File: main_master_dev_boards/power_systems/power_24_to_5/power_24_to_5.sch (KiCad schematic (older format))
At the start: 23 parts, among them J1 Switch_in, J2 24_in, J3 GND_in, J4 PGood_out, J5 ref_out, J6 5_out, J7 GND_out, U1 LMR16030

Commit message: Started Adding 3v3 power LDO to 24_to_5 dev board
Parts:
- added C5: 22uF, Capacitors_SMD:C_0603, symbol C
- added C6: 22uF, Capacitors_SMD:C_0603, symbol CP1
- added D3: GRN_LED, LEDs:LED_0603, symbol LED-RESCUE-main_master_board
- added J8: 3v3_out, Pin_Headers:Pin_Header_Straight_1x01_Pitch2.54mm, symbol CONN_01X01
- added J9: PGoodBackup_out, Pin_Headers:Pin_Header_Straight_1x01_Pitch2.54mm, symbol CONN_01X01
- added R8: 10, Resistors_SMD:R_0603, symbol R
- added U2: 74AUC1G32, SO-70:SO-70, symbol 74AUC1G32
- added U3: LP3852-3.3, SOT-223:SOT-223, symbol LP3852-3.3
- J4: value PGood_out -> PGoodMain_out
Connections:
- net labels added: 3V3, 3V3_out, PG_v5_backup, v5_good
- wire segments 49 -> 67
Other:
- note added: "5V to 3.3V LDO"
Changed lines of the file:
@@
 LIBS:contrib
 LIBS:valves
-LIBS:antenna
-LIBS:AS1360
-LIBS:conn_2x45
-LIBS:conn_2x50
-LIBS:conn_open_q_x2
-LIBS:esd7c5
-LIBS:FDS4935A
-LIBS:FPF1203LUCX
-LIBS:lan9512
-LIBS:LMR16020
-LIBS:LP3852-3.3
-LIBS:LTC2955-1
-LIBS:MIC2026
-LIBS:Si1077X
-LIBS:Si1900DL
-LIBS:SN74LV1T125
-LIBS:SN74LV4T125
-LIBS:TDP6E001RSER
-LIBS:tps82084sil
-LIBS:TPS754
-LIBS:TPS61089
-LIBS:TPS61232DRC
-LIBS:TPS832130SIL
-LIBS:0s102011ma1qn1
-LIBS:74LVC1G17
-LIBS:74V1T126
-LIBS:acs711klctr-12ab-t
-LIBS:AD7192
-LIBS:AD7193
-LIBS:am-hrr30-xxx
-LIBS:aon7528
-LIBS:AP7363
-LIBS:AS1359
-LIBS:csd16323q3
-LIBS:dmn2004dmk
-LIBS:dp_devices
-LIBS:DSPIC33E128MC506
-LIBS:fds6898az
-LIBS:ina197
-LIBS:irf7329pbf
-LIBS:ld1117
-LIBS:lm3478
-LIBS:lm3481
-LIBS:lt1910
-LIBS:ltc1871
-LIBS:ltc1982
-LIBS:MAG3110
-LIBS:mcp1700
-LIBS:mcp73831
-LIBS:mcsmt-g5030a1-3712
-LIBS:microchip_can
-LIBS:microclasp_hdrx2
-LIBS:microclasp_hdrx3
-LIBS:MPU-6000_MPU-6050
-LIBS:MPU-9150
-LIBS:nrf24l01+
-LIBS:pds1040l
-LIBS:pic12f1571
-LIBS:pinhead
-LIBS:psmn013-80ys
-LIBS:RESISTOR_ARRAY
-LIBS:rf803d
-LIBS:RGB_LED
-LIBS:Si1970DH
-LIBS:sn65hvd232
-LIBS:ssc54
-LIBS:sw_push_4
-LIBS:tc74
-LIBS:tps54540
-LIBS:TPS2113A
-LIBS:vs-mbrb1635pbf
-LIBS:xal5050-562meb
-LIBS:xal6030-182mec
-LIBS:ld29150dt50r
-LIBS:ncp59151ds50r4g
-LIBS:pinhd-2x23
+LIBS:main_master_board-cache
 LIBS:power_24_to_5-cache
 EELAYER 25 0
@@
 P 7740 3790
 F 0 "J4" H 7740 3890 50  0000 C CNN
-F 1 "PGood_out" V 7840 3790 50  0000 C CNN
+F 1 "PGoodMain_out" V 7840 3790 50  0000 C CNN
 F 2 "Pin_Headers:Pin_Header_Straight_1x01_Pitch2.54mm" H 7740 3790 50  0001 C CNN
 F 3 "" H 7740 3790 50  0001 C CNN
@@
 Wire Wire Line
 	1030 2720 1490 2720
+Text Notes 4580 4165 0    60   ~ 0
+5V to 3.3V LDO
+$Comp
+L LED-RESCUE-main_master_board D3
+U 1 1 59235EB5
+P 5100 4405
+F 0 "D3" H 5100 4505 50  0000 C CNN
+F 1 "GRN_LED" H 5100 4305 50  0000 C CNN
+F 2 "LEDs:LED_0603" H 5100 4405 50  0001 C CNN
+F 3 "http://www.digikey.com/product-detail/en/kingbright/APT1608ZGC/754-1126-1-ND" H 5100 4405 50  0001 C CNN
+	1    5100 4405
+	-1   0    0    1
+$EndComp
+$Comp
+L R R8
+U 1 1 59235EBC
+P 5500 4405
+F 0 "R8" V 5580 4405 50  0000 C CNN
+F 1 "10" V 5500 4405 50  0000 C CNN
+F 2 "Resistors_SMD:R_0603" V 5430 4405 50  0001 C CNN
+F 3 "" H 5500 4405 50  0000 C CNN
+	1    5500 4405
+	0    1    1    0
+$EndComp
+Text Label 4710 4405 0    60   ~ 0
+3V3
+$Comp
+L LP3852-3.3 U3
+U 1 1 59235EC4
+P 5850 4975
+F 0 "U3" H 6100 5225 50  0000 C CNN
+F 1 "LP3852-3.3" H 5800 5225 50  0000 C CNN
+F 2 "SOT-223:SOT-223" H 5600 4725 50  0001 C CNN
+F 3 "http://www.ti.com/lit/ds/symlink/lp3852.pdf" H 6200 4725 50  0001 C CNN
+	1    5850 4975
+	1    0    0    -1
+$EndComp
+Text Label 5890 5565 0    60   ~ 0
+GND
+$Comp
+L C C5
+U 1 1 59235ECD
+P 4830 5185
+F 0 "C5" H 4855 5285 50  0000 L CNN
+F 1 "22uF" H 4855 5085 50  0000 L CNN
+F 2 "Capacitors_SMD:C_0603" H 4868 5035 50  0001 C CNN
+F 3 "" H 4830 5185 50  0000 C CNN
+F 4 "10V" H 4730 5085 60  0000 C CNN "Voltage"
+	1    4830 5185
+	1    0    0    -1
+$EndComp
+$Comp
+L CP1 C6
+U 1 1 59235ED4
+P 6680 5185
+F 0 "C6" H 6705 5285 50  0000 L CNN
+F 1 "22uF" H 6705 5085 50  0000 L CNN
+F 2 "Capacitors_SMD:C_0603" H 6680 5185 50  0001 C CNN
+F 3 "" H 6680 5185 50  0000 C CNN
+	1    6680 5185
+	1    0    0    -1
+$EndComp
+Text Label 6740 4825 0    60   ~ 0
+3V3_out
+Text Label 5700 4405 0    60   ~ 0
+GND
+Connection ~ 4830 4825
+Connection ~ 6680 4825
+Connection ~ 6680 5565
+Wire Wire Line
+	6680 5565 6680 5335
+Wire Wire Line
+	6680 4825 6680 5035
+Wire Wire Line
+	6400 4825 6920 4825
+Wire Wire Line
+	4600 5565 6900 5565
+Wire Wire Line
+	5850 5565 5850 5475
+Connection ~ 5850 5565
+Wire Wire Line
+	6460 4925 6400 4925
+Wire Wire Line
+	6460 5565 6460 4925
+Connection ~ 6460 5565
+Wire Wire Line
+	5300 4925 4930 4925
+Wire Wire Line
+	4600 4825 5300 4825
+Wire Wire Line
+	4830 4825 4830 5035
+Wire Wire Line
+	4830 5335 4830 5565
+Connection ~ 4830 5565
+Text Label 4950 4925 0    60   ~ 0
+v5_good
+Text Label 5200 5975 2    60   ~ 0
+PG_v5_main
+Text Label 5200 6075 2    60   ~ 0
+PG_v5_backup
+Wire Wire Line
+	5270 6075 4570 6075
+Wire Wire Line
+	5270 5975 4670 5975
+Wire Wire Line
+	5820 6025 6200 6025
+Text Label 5840 6025 0    60   ~ 0
+v5_good
+$Comp
+L 74AUC1G32 U2
+U 1 1 59235EF6
+P 5570 6025
+F 0 "U2" H 5470 6175 40  0000 C CNN
+F 1 "74AUC1G32" H 5570 5875 40  0000 C CNN
+F 2 "SO-70:SO-70" H 5570 6025 60  0001 C CNN
+F 3 "https://octopart.com/sn74auc1g32dckr-texas+instruments-464483" H 5570 6025 60  0001 C CNN
+	1    5570 6025
+	1    0    0    -1
+$EndComp
+Wire Wire Line
+	5300 4405 5350 4405
+Wire Wire Line
+	5650 4405 5890 4405
+Wire Wire Line
+	4900 4405 4620 4405
+Text Label 4640 4825 0    60   ~ 0
+V5_MAIN
+$Comp
+L CONN_01X01 J9
+U 1 1 592365BC
+P 7550 5965
+F 0 "J9" H 7550 6065 50  0000 C CNN
+F 1 "PGoodBackup_out" V 7650 5965 50  0000 C CNN
+F 2 "Pin_Headers:Pin_Header_Straight_1x01_Pitch2.54mm" H 7550 5965 50  0001 C CNN
+F 3 "" H 7550 5965 50  0001 C CNN
+	1    7550 5965
+	1    0    0    -1
+$EndComp
+Wire Wire Line
+	7350 5965 6870 5965
+Text Label 7320 5965 2    60   ~ 0
+PG_v5_backup
+$Comp
+L CONN_01X01 J8
+U 1 1 59236FA2
+P 7120 4825
+F 0 "J8" H 7120 4925 50  0000 C CNN
+F 1 "3v3_out" V 7220 4825 50  0000 C CNN
+F 2 "Pin_Headers:Pin_Header_Straight_1x01_Pitch2.54mm" H 7120 4825 50  0001 C CNN
+F 3 "" H 7120 4825 50  0001 C CNN
+	1    7120 4825
+	1    0    0    -1
+$EndComp
 $EndSCHEMATC

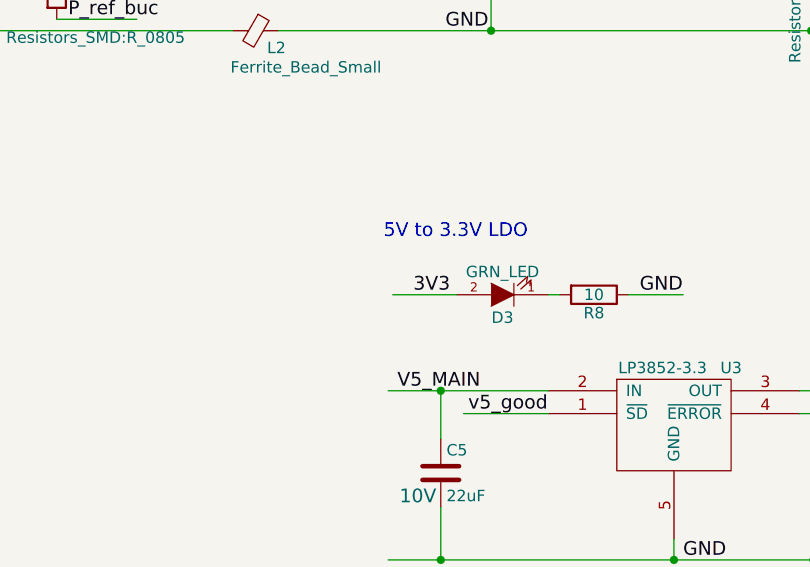
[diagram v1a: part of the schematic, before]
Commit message: Placed 3v3 LDO and components. Need to route
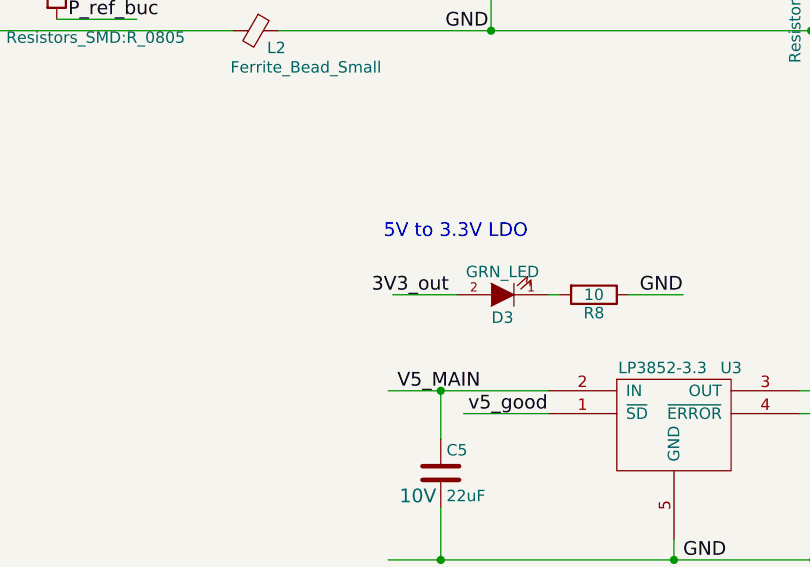
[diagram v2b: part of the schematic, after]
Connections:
- net labels removed: 3V3
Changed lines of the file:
@@
 	0    1    1    0
 $EndComp
-Text Label 4710 4405 0    60   ~ 0
-3V3
 $Comp
 L LP3852-3.3 U3
@@
 	1    0    0    -1
 $EndComp
+Text Label 4865 4405 2    60   ~ 0
+3V3_out
 $EndSCHEMATC
